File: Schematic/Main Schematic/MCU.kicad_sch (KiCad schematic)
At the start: 12 parts, among them J7 Conn_01x02_Pin, U4 M24C16-RMN6TP

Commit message: Updat
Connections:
- net 3.3V: now also C?.1, U?.16 (VCC)
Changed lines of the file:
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@@
   (junction (at 191.77 57.15) (diameter 0) (color 0 0 0 0)
+  )
+  (junction (at 94.5388 44.45) (diameter 0) (color 0 0 0 0)
+  )
+  (junction (at 94.5388 41.91) (diameter 0) (color 0 0 0 0)
   )
   (junction (at 186.69 67.31) (diameter 0) (color 0 0 0 0)
@@
     (stroke (width 0) (type default))
   )
-  (wire (pts (xy 93.98 41.91) (xy 100.33 41.91))
+  (wire (pts (xy 93.98 41.91) (xy 94.5388 41.91))
     (stroke (width 0) (type default))
   )
   (wire (pts (xy 102.87 52.07) (xy 100.33 52.07))
+    (stroke (width 0) (type default))
+  )
+  (wire (pts (xy 94.5388 44.45) (xy 95.25 44.45))
     (stroke (width 0) (type default))
   )
@@
   )
   (wire (pts (xy 52.07 54.61) (xy 63.5 54.61))
+    (stroke (width 0) (type default))
+  )
+  (wire (pts (xy 94.5388 41.91) (xy 100.33 41.91))
     (stroke (width 0) (type default))
   )
@@
     (stroke (width 0) (type default))
   )
+  (wire (pts (xy 94.5388 41.91) (xy 94.5388 44.45))
+    (stroke (width 0) (type default))
+  )
   (wire (pts (xy 241.3 59.69) (xy 250.19 59.69))
     (stroke (width 0) (type default))
@@
     (stroke (width 0) (type default))
   )
+  (wire (pts (xy 94.5388 44.45) (xy 94.5388 44.5008))
+    (stroke (width 0) (type default))
+  )
   (wire (pts (xy 48.26 49.53) (xy 49.53 49.53))
     (stroke (width 0) (type default))
@@
     (stroke (width 0) (type default))
   )
-  (wire (pts (xy 93.98 44.45) (xy 95.25 44.45))
+  (wire (pts (xy 93.98 44.45) (xy 94.5388 44.45))
     (stroke (width 0) (type default))
   )

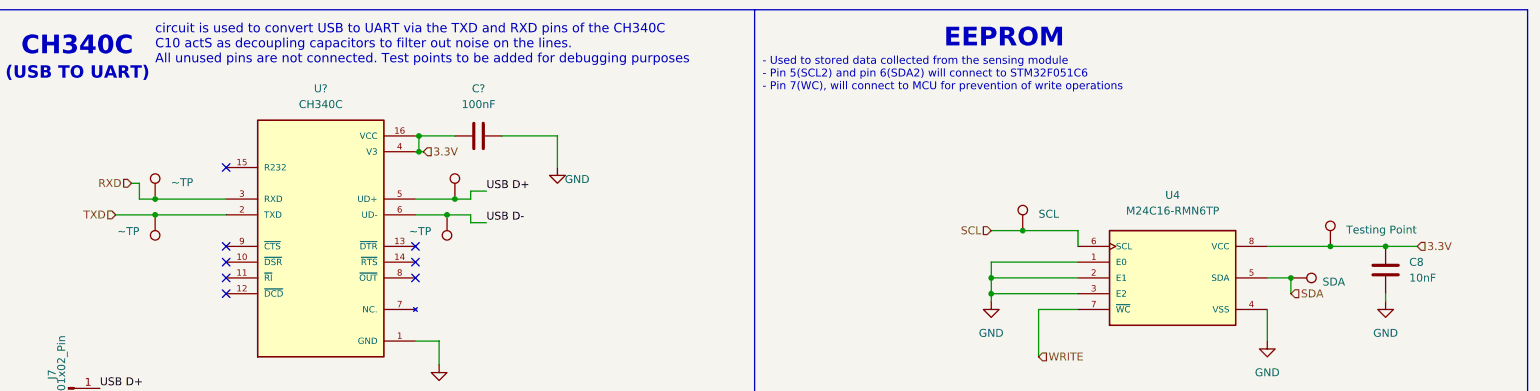
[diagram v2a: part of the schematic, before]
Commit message: Updated the footprints and the PCB
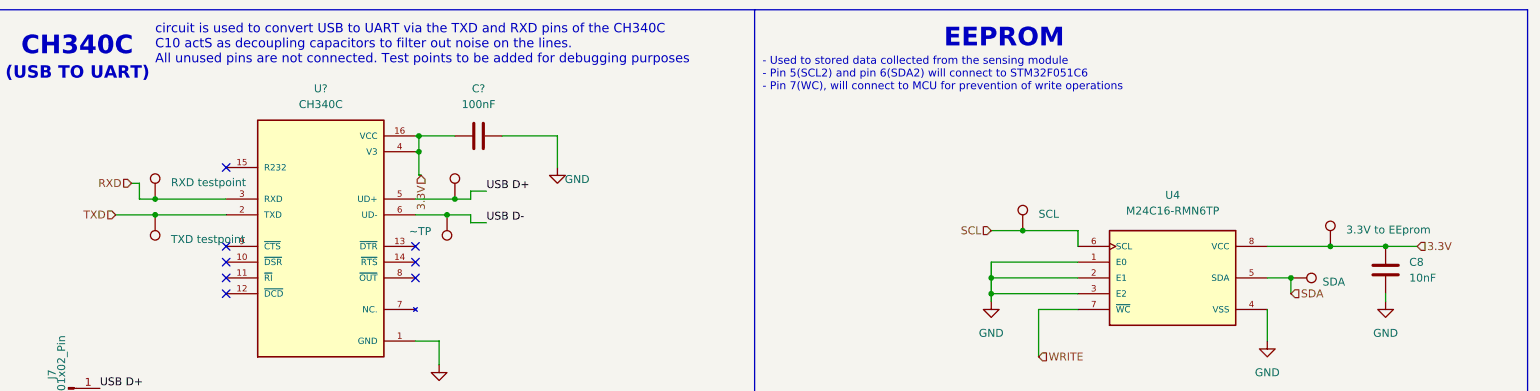
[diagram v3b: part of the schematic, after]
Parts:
- J7: footprint (none) -> Connector_PinHeader_2.54mm:PinHeader_1x02_P2.54mm_Vertical
- TP12: value Testing Point -> 3.3V to EEprom
- TP6: value ~TP -> RXD testpoint
- TP7: value ~TP -> TXD testpoint
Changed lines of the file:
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@@
   (junction (at 191.77 57.15) (diameter 0) (color 0 0 0 0)
   )
+  (junction (at 186.69 67.31) (diameter 0) (color 0 0 0 0)
+  )
+  (junction (at 250.19 59.69) (diameter 0) (color 0 0 0 0)
+  )
+  (junction (at 234.95 64.77) (diameter 0) (color 0 0 0 0)
+  )
+  (junction (at 186.69 64.77) (diameter 0) (color 0 0 0 0)
+  )
+  (junction (at 94.5388 41.91) (diameter 0) (color 0 0 0 0)
+  )
   (junction (at 94.5388 44.45) (diameter 0) (color 0 0 0 0)
-  )
-  (junction (at 94.5388 41.91) (diameter 0) (color 0 0 0 0)
-  )
-  (junction (at 186.69 67.31) (diameter 0) (color 0 0 0 0)
-  )
-  (junction (at 250.19 59.69) (diameter 0) (color 0 0 0 0)
-  )
-  (junction (at 234.95 64.77) (diameter 0) (color 0 0 0 0)
-  )
-  (junction (at 186.69 64.77) (diameter 0) (color 0 0 0 0)
   )
   (junction (at 52.07 52.07) (diameter 0) (color 0 0 0 0)
@@
     (stroke (width 0) (type default))
   )
-  (wire (pts (xy 94.5388 44.45) (xy 95.25 44.45))
-    (stroke (width 0) (type default))
-  )
   (wire (pts (xy 93.98 74.93) (xy 97.79 74.93))
     (stroke (width 0) (type default))
   )
+  (wire (pts (xy 94.5388 48.2092) (xy 94.8944 48.2092))
+    (stroke (width 0) (type default))
+  )
   (wire (pts (xy 52.07 54.61) (xy 63.5 54.61))
     (stroke (width 0) (type default))
@@
     (stroke (width 0) (type default))
   )
+  (wire (pts (xy 94.5388 44.45) (xy 94.5388 48.2092))
+    (stroke (width 0) (type default))
+  )
   (wire (pts (xy 186.69 64.77) (xy 186.69 67.31))
     (stroke (width 0) (type default))
@@
     (stroke (width 0) (type default))
   )
-  (wire (pts (xy 94.5388 44.45) (xy 94.5388 44.5008))
-    (stroke (width 0) (type default))
-  )
   (wire (pts (xy 48.26 49.53) (xy 49.53 49.53))
     (stroke (width 0) (type default))
@@
   )
   (wire (pts (xy 186.69 67.31) (xy 186.69 68.58))
+    (stroke (width 0) (type default))
+  )
+  (wire (pts (xy 94.8944 48.2092) (xy 94.8944 48.26))
     (stroke (width 0) (type default))
   )
@@
     (effects (font (size 1.27 1.27)) (justify right))
   )
-  (hierarchical_label "3.3V" (shape input) (at 95.25 44.45 0) (fields_autoplaced)
-    (effects (font (size 1.27 1.27)) (justify left))
+  (hierarchical_label "3.3V" (shape input) (at 94.8944 48.26 270) (fields_autoplaced)
+    (effects (font (size 1.27 1.27)) (justify right))
   )
   (hierarchical_label "RXD" (shape input) (at 48.26 49.53 180) (fields_autoplaced)
@@
       (effects (font (size 1.27 1.27)) (justify left) hide)
     )
-    (property "Value" "~TP" (at 49.53 57.277 0)
-      (effects (font (size 1.27 1.27)) (justify left))
+    (property "Value" "TXD testpoint" (at 54.61 58.547 0)
+      (effects (font (size 1.27 1.27)) (justify right))
     )
     (property "Footprint" "TestPoint:TestPoint_Pad_1.0x1.0mm" (at 46.99 54.61 0)
@@
       (effects (font (size 1.27 1.27)) (justify left) hide)
     )
-    (property "Value" "~TP" (at 54.61 49.403 0)
+    (property "Value" "RXD testpoint" (at 54.61 49.403 0)
       (effects (font (size 1.27 1.27)) (justify left))
     )
@@
       (effects (font (size 1.27 1.27)))
     )
-    (property "Footprint" "" (at 38.1 82.55 0)
+    (property "Footprint" "Connector_PinHeader_2.54mm:PinHeader_1x02_P2.54mm_Vertical" (at 38.1 82.55 0)
       (effects (font (size 1.27 1.27)) hide)
     )
@@
       (effects (font (size 1.27 1.27)) (justify left) hide)
     )
-    (property "Value" "Testing Point" (at 243.84 57.023 0)
+    (property "Value" "3.3V to EEprom" (at 243.84 57.023 0)
       (effects (font (size 1.27 1.27)) (justify left))
     )

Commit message: Updated
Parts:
- U4: footprint LM75AD:SOIC127P600X175-8N -> M24C16-RMN6TP:SOIC127P600X175-8N
- U?: footprint CH340:SOIC127P600X180-16N -> CH340C:SOIC127P600X180-16N
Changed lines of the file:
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@@
   (symbol (lib_id "CH340C:CH340C") (at 78.74 59.69 0) (unit 1)
     (in_bom yes) (on_board yes) (dnp no) (fields_autoplaced)
-    (property "Reference" "U?" (at 78.74 34.29 0)
+    (property "Reference" "U?" (at 78.74 35.56 0)
       (effects (font (size 1.27 1.27)))
     )
-    (property "Value" "CH340C" (at 78.74 36.83 0)
+    (property "Value" "CH340C" (at 78.74 38.1 0)
       (effects (font (size 1.27 1.27)))
     )
-    (property "Footprint" "CH340:SOIC127P600X180-16N" (at 78.74 59.69 0)
-      (effects (font (size 1.27 1.27)) (justify left bottom) hide)
+    (property "Footprint" "CH340C:SOIC127P600X180-16N" (at 78.74 59.69 0)
+      (effects (font (size 1.27 1.27)) (justify bottom) hide)
     )
     (property "Datasheet" "" (at 78.74 59.69 0)
-      (effects (font (size 1.27 1.27)) (justify left bottom) hide)
+      (effects (font (size 1.27 1.27)) hide)
     )
     (property "MANUFACTURER" "WCH" (at 78.74 59.69 0)
-      (effects (font (size 1.27 1.27)) (justify left bottom) hide)
+      (effects (font (size 1.27 1.27)) (justify bottom) hide)
     )
     (property "PARTREV" "2G" (at 78.74 59.69 0)
-      (effects (font (size 1.27 1.27)) (justify left bottom) hide)
+      (effects (font (size 1.27 1.27)) (justify bottom) hide)
     )
     (property "MAXIMUM_PACKAGE_HEIGHT" "1.8 mm" (at 78.74 59.69 0)
-      (effects (font (size 1.27 1.27)) (justify left bottom) hide)
+      (effects (font (size 1.27 1.27)) (justify bottom) hide)
     )
     (property "STANDARD" "IPC 7351B" (at 78.74 59.69 0)
-      (effects (font (size 1.27 1.27)) (justify left bottom) hide)
+      (effects (font (size 1.27 1.27)) (justify bottom) hide)
     )
     (pin "1")
@@
       (effects (font (size 1.27 1.27)))
     )
-    (property "Footprint" "LM75AD:SOIC127P600X175-8N" (at 215.9 64.77 0)
+    (property "Footprint" "M24C16-RMN6TP:SOIC127P600X175-8N" (at 215.9 64.77 0)
       (effects (font (size 1.27 1.27)) (justify left bottom) hide)
     )

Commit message: Update
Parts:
- C?: footprint 100NF_C:CAPC1005X55N -> A_New_folder:C1206
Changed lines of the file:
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@@
       (effects (font (size 1.27 1.27)))
     )
-    (property "Footprint" "100NF_C:CAPC1005X55N" (at 107.95 40.9448 0)
+    (property "Footprint" "A_New_folder:C1206" (at 107.95 40.9448 0)
       (effects (font (size 1.27 1.27)) hide)
     )

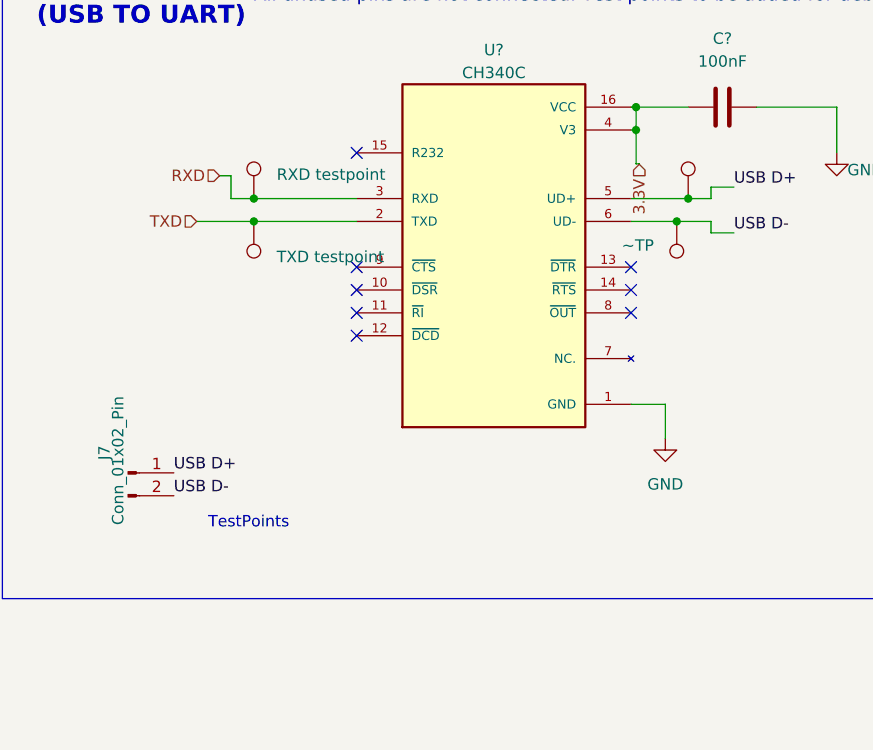
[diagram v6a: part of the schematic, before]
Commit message: Footprints all added and the PCB has been created but not placed according to the proper configuration
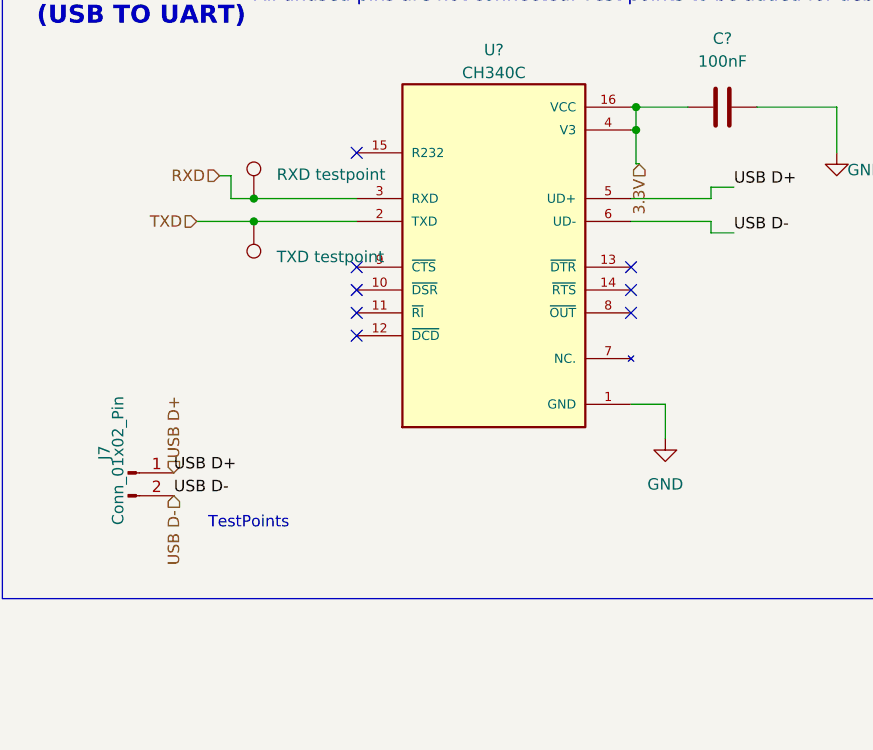
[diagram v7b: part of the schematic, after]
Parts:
- removed TP8: ~TP, TestPoint:TestPoint_Pad_1.0x1.0mm, symbol Connector:TestPoint
- removed TP9: ~, TestPoint:TestPoint_Pad_1.0x1.0mm, symbol Connector:TestPoint
- C8: footprint CAP_10NF:CAPC1005X55N -> A_New_folder:C1206
- U4: footprint M24C16-RMN6TP:SOIC127P600X175-8N -> A_New_folder:SOIC-8_L5.0-W4.0-P1.27-LS6.0-BL
- U?: footprint CH340C:SOIC127P600X180-16N -> A_New_folder:SOP-16_L10.0-W3.9-P1.27-LS6.0-BL
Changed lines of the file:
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@@
   (junction (at 52.07 52.07) (diameter 0) (color 0 0 0 0)
   )
-  (junction (at 100.33 52.07) (diameter 0) (color 0 0 0 0)
-  )
   (junction (at 241.3 59.69) (diameter 0) (color 0 0 0 0)
   )
   (junction (at 52.07 54.61) (diameter 0) (color 0 0 0 0)
-  )
-  (junction (at 99.06 54.61) (diameter 0) (color 0 0 0 0)
   )
   (no_connect (at 63.5 67.31))
@@
     (stroke (width 0) (type default))
   )
-  (wire (pts (xy 102.87 52.07) (xy 100.33 52.07))
+  (wire (pts (xy 93.98 52.07) (xy 102.87 52.07))
     (stroke (width 0) (type default))
   )
@@
     (stroke (width 0) (type default))
   )
-  (wire (pts (xy 99.06 54.61) (xy 102.87 54.61))
-    (stroke (width 0) (type default))
-  )
   (wire (pts (xy 200.66 57.15) (xy 200.66 59.69))
     (stroke (width 0) (type default))
@@
     (stroke (width 0) (type default))
   )
-  (wire (pts (xy 93.98 54.61) (xy 99.06 54.61))
+  (wire (pts (xy 93.98 54.61) (xy 102.87 54.61))
     (stroke (width 0) (type default))
   )
@@
   )
   (wire (pts (xy 93.98 44.45) (xy 94.5388 44.45))
-    (stroke (width 0) (type default))
-  )
-  (wire (pts (xy 100.33 52.07) (xy 93.98 52.07))
     (stroke (width 0) (type default))
   )
@@
     (effects (font (size 1.27 1.27)) (justify right))
   )
+  (hierarchical_label "USB D+" (shape input) (at 43.18 82.55 90) (fields_autoplaced)
+    (effects (font (size 1.27 1.27)) (justify left))
+  )
+  (hierarchical_label "USB D-" (shape input) (at 43.18 85.09 270) (fields_autoplaced)
+    (effects (font (size 1.27 1.27)) (justify right))
+  )
   (hierarchical_label "SDA" (shape input) (at 234.95 67.31 0) (fields_autoplaced)
     (effects (font (size 1.27 1.27)) (justify left))
@@
     )
   )
-  (symbol (lib_id "Connector:TestPoint") (at 99.06 54.61 180) (unit 1)
-    (in_bom yes) (on_board yes) (dnp no) (fields_autoplaced)
-    (property "Reference" "TP8" (at 100.3301 59.69 90)
-      (effects (font (size 1.27 1.27)) (justify left) hide)
-    )
-    (property "Value" "~TP" (at 96.52 57.277 0)
-      (effects (font (size 1.27 1.27)) (justify left))
-    )
-    (property "Footprint" "TestPoint:TestPoint_Pad_1.0x1.0mm" (at 93.98 54.61 0)
-      (effects (font (size 1.27 1.27)) hide)
-    )
-    (property "Datasheet" "~" (at 93.98 54.61 0)
-      (effects (font (size 1.27 1.27)) hide)
-    )
-    (pin "1")
-    (instances
-      (project "Main Schematic"
-        (path "/81c41bad-bb43-41af-b405-18d135a809b1/ae15d31d-f7b4-4051-b9d0-3a01939afe0e"
-          (reference "TP8") (unit 1)
-        )
-      )
-      (project "main"
-        (path "/e63e39d7-6ac0-4ffd-8aa3-1841a4541b55/59b42903-2dc7-4011-ab5b-d7b81bd233c3"
-          (reference "TP?") (unit 1)
-        )
-      )
-    )
-  )
   (symbol (lib_id "Connector:TestPoint") (at 234.95 64.77 270) (unit 1)
     (in_bom yes) (on_board yes) (dnp no) (fields_autoplaced)
@@
     )
   )
-  (symbol (lib_id "Connector:TestPoint") (at 100.33 52.07 0) (unit 1)
-    (in_bom yes) (on_board yes) (dnp no) (fields_autoplaced)
-    (property "Reference" "TP9" (at 99.0599 46.99 90)
-      (effects (font (size 1.27 1.27)) (justify left) hide)
-    )
-    (property "Value" "~" (at 102.87 49.403 0)
-      (effects (font (size 1.27 1.27)) (justify left))
-    )
-    (property "Footprint" "TestPoint:TestPoint_Pad_1.0x1.0mm" (at 105.41 52.07 0)
-      (effects (font (size 1.27 1.27)) hide)
-    )
-    (property "Datasheet" "~" (at 105.41 52.07 0)
-      (effects (font (size 1.27 1.27)) hide)
-    )
-    (pin "1")
-    (instances
-      (project "Main Schematic"
-        (path "/81c41bad-bb43-41af-b405-18d135a809b1/ae15d31d-f7b4-4051-b9d0-3a01939afe0e"
-          (reference "TP9") (unit 1)
-        )
-      )
-      (project "main"
-        (path "/e63e39d7-6ac0-4ffd-8aa3-1841a4541b55/59b42903-2dc7-4011-ab5b-d7b81bd233c3"
-          (reference "TP?") (unit 1)
-        )
-      )
-    )
-  )
   (symbol (lib_id "CH340C:CH340C") (at 78.74 59.69 0) (unit 1)
     (in_bom yes) (on_board yes) (dnp no) (fields_autoplaced)
@@
       (effects (font (size 1.27 1.27)))
     )
-    (property "Footprint" "CH340C:SOIC127P600X180-16N" (at 78.74 59.69 0)
+    (property "Footprint" "A_New_folder:SOP-16_L10.0-W3.9-P1.27-LS6.0-BL" (at 78.74 59.69 0)
       (effects (font (size 1.27 1.27)) (justify bottom) hide)
     )
@@
       (effects (font (size 1.27 1.27)) (justify left))
     )
-    (property "Footprint" "CAP_10NF:CAPC1005X55N" (at 251.1552 67.31 0)
+    (property "Footprint" "A_New_folder:C1206" (at 251.1552 67.31 0)
       (effects (font (size 1.27 1.27)) hide)
     )
@@
       (effects (font (size 1.27 1.27)))
     )
-    (property "Footprint" "M24C16-RMN6TP:SOIC127P600X175-8N" (at 215.9 64.77 0)
+    (property "Footprint" "A_New_folder:SOIC-8_L5.0-W4.0-P1.27-LS6.0-BL" (at 215.9 64.77 0)
       (effects (font (size 1.27 1.27)) (justify left bottom) hide)
     )

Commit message: Update
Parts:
- TP11: value SDA -> SDL
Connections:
- net SDA renamed SDL
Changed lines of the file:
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@@
     (effects (font (size 1.27 1.27)) (justify right))
   )
-  (hierarchical_label "SDA" (shape input) (at 234.95 67.31 0) (fields_autoplaced)
+  (hierarchical_label "SDL" (shape input) (at 234.95 67.31 0) (fields_autoplaced)
     (effects (font (size 1.27 1.27)) (justify left))
   )
@@
       (effects (font (size 1.27 1.27)) (justify left) hide)
     )
-    (property "Value" "SDA" (at 240.03 65.405 90)
+    (property "Value" "SDL" (at 240.03 65.405 90)
       (effects (font (size 1.27 1.27)) (justify left))
     )
